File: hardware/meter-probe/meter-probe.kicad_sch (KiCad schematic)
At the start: 36 parts, among them J1 Cable, J2 Cable, Q1 BSS138, SW1 Sensor Button, U2 TC1301A-APA, U3 TCA9517A, U4 USBLC6-2SC6, U5 M24C02-D, U6 TSL2585

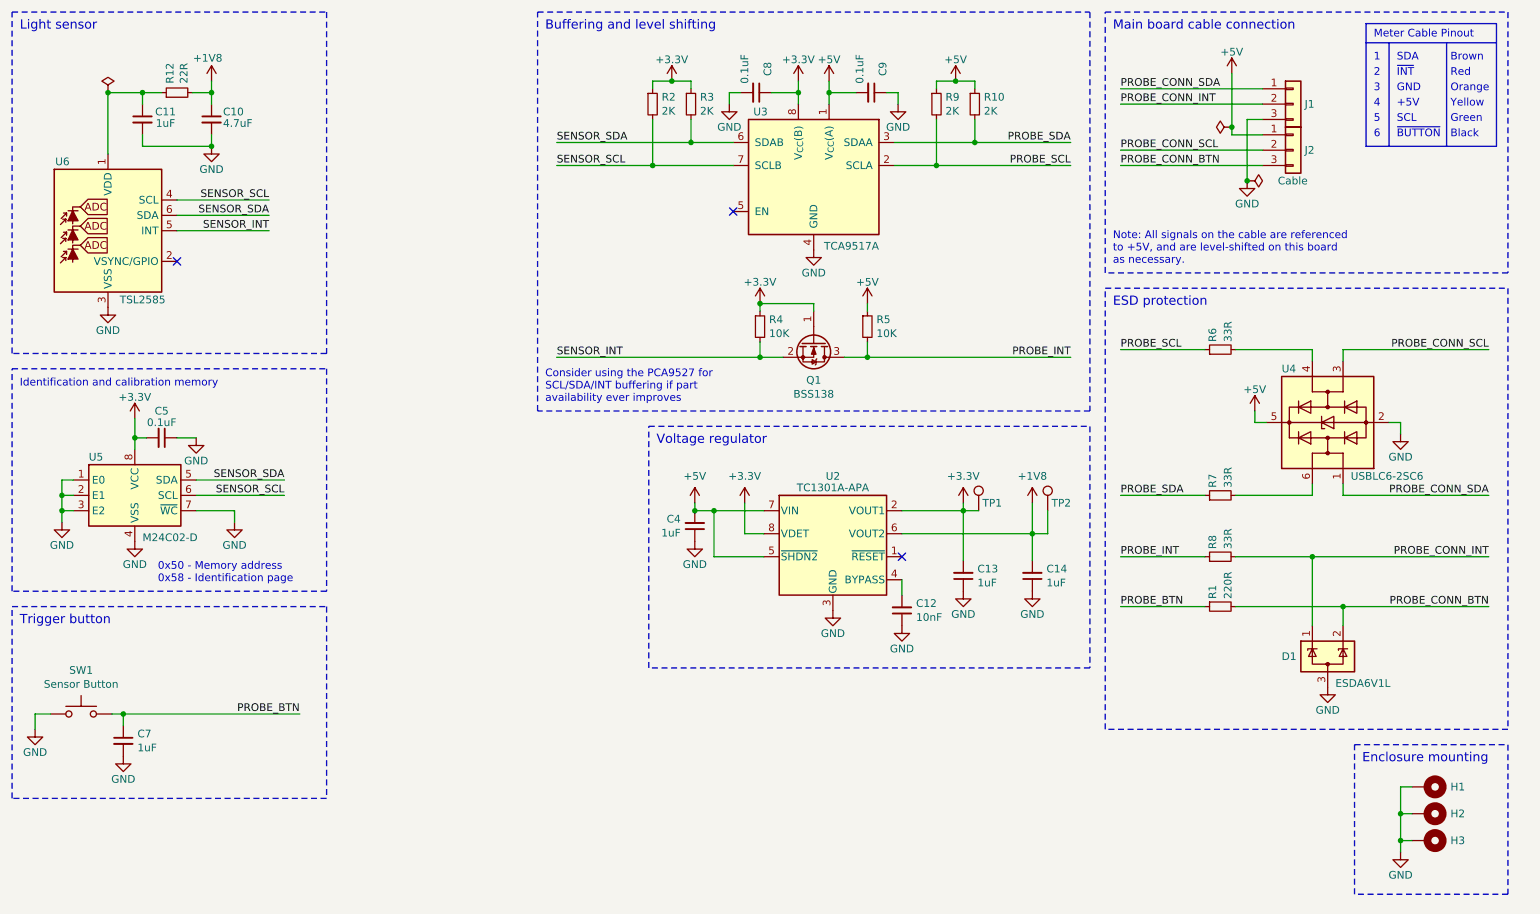
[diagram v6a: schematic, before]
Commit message: Re-assign reference designators and add fiducials
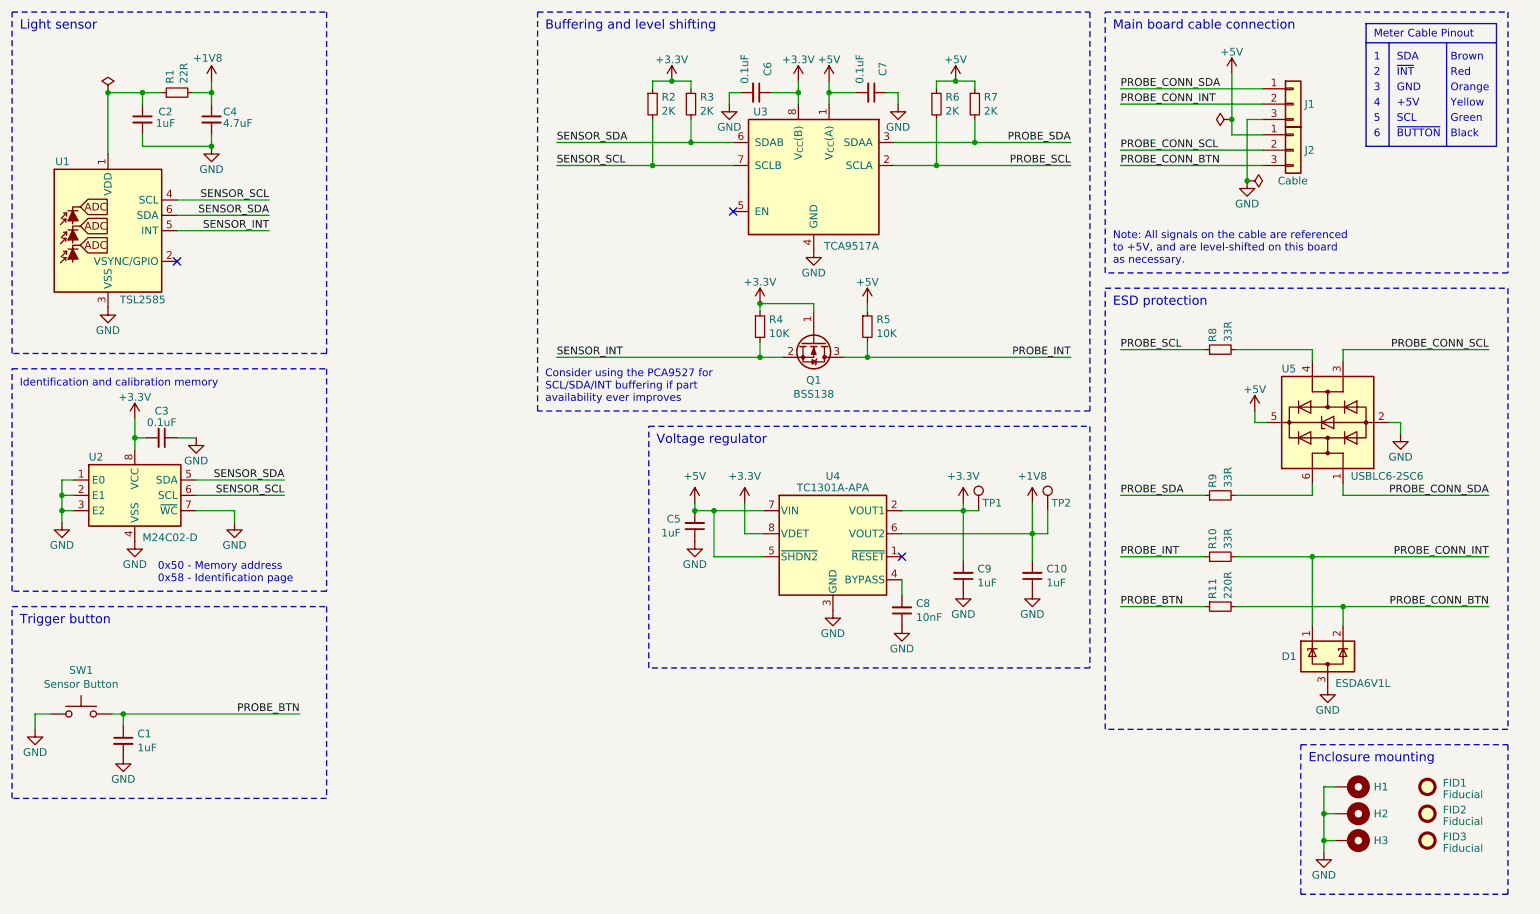
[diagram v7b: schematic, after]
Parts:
- added FID1, FID2, FID3: Fiducial, Fiducial:Fiducial_1mm_Mask2mm, symbol Mechanical:Fiducial
- renumbered C7 to C1, C14 to C10, C11 to C2, C5 to C3, C10 to C4, C4 to C5, C8 to C6, C9 to C7, C12 to C8, C13 to C9, R12 to R1, R8 to R10, R1 to R11, R9 to R6, R10 to R7, R6 to R8, R7 to R9, U6 to U1, U5 to U2, U2 to U4, U4 to U5
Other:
- moved on the sheet: H1, H2, H3

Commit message: Fill out BOM data for light sensor
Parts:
- U1: Manufacturer (none) -> ams OSRAM; Manufacturer PN (none) -> TSL25853PM; Supplier (none) -> Digi-Key; Supplier PN (none) -> 4991-TSL25853PMCT-ND
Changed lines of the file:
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@@
       (effects (font (size 1.27 1.27)) hide)
     )
-    (property "Description" "" (at 31.75 52.07 0)
+    (property "Description" "AMBIENT LIGHT SENSOR" (at 31.75 52.07 0)
       (effects (font (size 1.27 1.27)) hide)
     )
-    (property "Manufacturer" "" (at 31.75 52.07 0)
+    (property "Manufacturer" "ams OSRAM" (at 31.75 52.07 0)
       (effects (font (size 1.27 1.27)) hide)
     )
-    (property "Manufacturer PN" "" (at 31.75 52.07 0)
+    (property "Manufacturer PN" "TSL25853PM" (at 31.75 52.07 0)
       (effects (font (size 1.27 1.27)) hide)
     )
-    (property "Supplier" "" (at 31.75 52.07 0)
+    (property "Supplier" "Digi-Key" (at 31.75 52.07 0)
       (effects (font (size 1.27 1.27)) hide)
     )
-    (property "Supplier PN" "" (at 31.75 52.07 0)
+    (property "Supplier PN" "4991-TSL25853PMCT-ND" (at 31.75 52.07 0)
       (effects (font (size 1.27 1.27)) hide)
     )
